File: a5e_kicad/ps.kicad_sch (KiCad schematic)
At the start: 51 parts, among them U15 TDA38812XUMA1

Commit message: Add LCSC part numbers and fix C102 footprint
Add a hidden LCSC field to 290 symbols from the JLCPCB parts match
(2026-10-23). Left without LCSC: U7, U15, L1 (not in the JLCPCB
library), C1/C2/C4 and L2-L5 (no value specified), J3 (no confident
match) and Y3 (the 12 pF Basic crystal does not suit the 27 pF load
caps). U2, U12, Y2 and J9 carry the exact-MPN LCSC numbers although
they currently show zero JLCPCB stock.

C102 (22U 6V3) had a 0201 footprint; no 22 uF 0201 part exists. Change
it to 0402 (C415703) like C5-C7.
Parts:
- C122, C133, C134, C135, C136, C137, C138, C139, C140, C141, C142, C143, C144, C145, C146, C147, C148, C149, C150, C151, C152, C153, C154, C155, C156: LCSC (none) -> C190183
- C123, C129, C130, C131, C132, C5, C6, C7: LCSC (none) -> C415703
- C124: LCSC (none) -> C84494
- C198: LCSC (none) -> C1530
- C199, C200: LCSC (none) -> C327019
- C201, C224, C225, C226, C227: LCSC (none) -> C12530
- C202: LCSC (none) -> C1525
- R1: LCSC (none) -> C25783
- R2: LCSC (none) -> C25744
- R55, R58: LCSC (none) -> C25908
- R56: LCSC (none) -> C132339
- R57: LCSC (none) -> C36871

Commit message: VCORE: PGOOD pull-up off 5V0 (abs max 4 V), L1 rated for the OCP limit
Checked the TDA38812 stage against its data sheet (V2.1). MODE gives
1 MHz FCCM, OCP valley is 10.7 A typ / 12.4 A max with R55 5.6k,
soft-start is 2.2 ms, and the output is 0.754 V; the load is 6-7 A worst
case per Quartus.

- R58: PGOOD was pulled to 5V0, but its absolute maximum is 4.0 V. It is
  now 10k (>= 10k per the data sheet) to the TDA38812 VCC LDO (3.0 V,
  net tda_vcc). The AP61202 EN threshold is 0.91 V.
- L1: needs Isat >= OCPmax + ripple ~ 15.3 A. The Cyntec CMLE051H had no
  LCSC number and an unknown rating. It is now the Tai-Tech
  TMPC0503H-R22MG-D (C357176, 220 nH, Isat 21 A, 3.7 mOhm), with a new
  footprint agilex_lib:L_TaiTech_TMPC0503H from the data sheet land
  pattern.
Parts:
- L1: value 250n -> 220n; footprint agilex_lib:CMLE051H -> agilex_lib:L_TaiTech_TMPC0503H; LCSC (none) -> C357176
- R58: value 5.6k -> 10k; LCSC C25908 -> C25744
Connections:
- net 5V0: no longer R58.1
- net tda_vcc: now reaches C201.2, U15.19 (VCC)
- net tda_vcc: now also R58.1
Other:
- note added: "R58 PGOOD pull-up to the TDA38812 VCC LDO (3.0 V): PGOOD abs max is 4.0 V, so not 5V0. L1: Isat >= OCPmax + ripple = 12.4 A + 2.9 A (R55 5.6k, 1 MHz FCCM via R56||R57 = 60.6k)"
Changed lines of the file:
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@@
 	)
 	(junction
-		(at 100.33 60.96)
-		(diameter 0)
-		(color 0 0 0 0)
-	)
-	(junction
 		(at 208.28 44.45)
 		(diameter 0)
@@
 	(wire
 		(pts
-			(xy 100.33 67.31) (xy 100.33 60.96)
-		)
-		(stroke
-			(width 0)
-			(type default)
-		)
-	)
-	(wire
-		(pts
 			(xy 128.27 137.16) (xy 148.59 137.16)
 		)
@@
 			)
 		)
-		(property "Value" "250n"
+		(property "Value" "220n"
 			(at 195.58 68.58 90)
 			(show_name no)
@@
 			)
 		)
-		(property "Footprint" "agilex_lib:CMLE051H"
+		(property "LCSC" "C357176"
+			(at 195.58 71.12 0)
+			(hide yes)
+			(show_name no)
+			(do_not_autoplace no)
+			(effects
+				(font
+					(size 1.27 1.27)
+				)
+			)
+		)
+		(property "Footprint" "agilex_lib:L_TaiTech_TMPC0503H"
 			(at 195.58 71.12 0)
 			(hide yes)
@@
 			)
 		)
-		(property "Description" "Inductor"
+		(property "Description" "Tai-Tech TMPC0503H-R22MG-D, 220 nH, Isat 21 A, Irms 15.5 A, 3.7 mOhm"
 			(at 195.58 71.12 0)
 			(hide yes)
@@
 			)
 		)
-		(property "Value" "5.6k"
+		(property "Value" "10k"
 			(at 102.87 72.3899 0)
 			(show_name no)
@@
 			)
 		)
-		(property "LCSC" "C25908"
+		(property "LCSC" "C25744"
 			(at 98.552 71.12 90)
 			(hide yes)
@@
 		)
 	)
+	(wire
+		(pts
+			(xy 100.33 67.31) (xy 100.33 64.77)
+		)
+		(stroke
+			(width 0)
+			(type default)
+		)
+	)
+	(label "tda_vcc"
+		(at 100.33 64.77 0)
+		(effects
+			(font
+				(size 1.27 1.27)
+			)
+			(justify left bottom)
+		)
+	)
+	(label "tda_vcc"
+		(at 123.19 64.77 0)
+		(effects
+			(font
+				(size 1.27 1.27)
+			)
+			(justify left bottom)
+		)
+	)
+	(text "R58 PGOOD pull-up to the TDA38812 VCC LDO (3.0 V): PGOOD abs max is 4.0 V, so not 5V0.\nL1: Isat >= OCPmax + ripple = 12.4 A + 2.9 A (R55 5.6k, 1 MHz FCCM via R56||R57 = 60.6k)"
+		(exclude_from_sim no)
+		(at 60.96 40.64 0)
+		(effects
+			(font
+				(size 1.27 1.27)
+			)
+			(justify left)
+		)
+	)

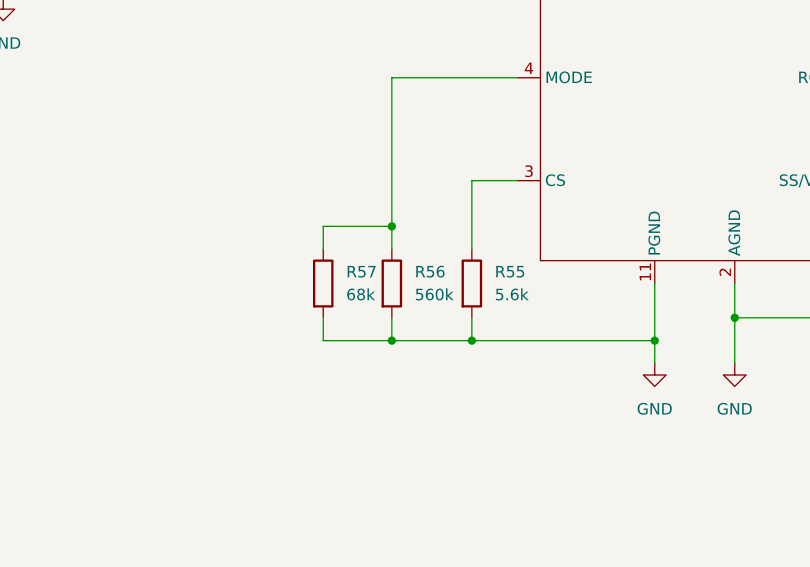
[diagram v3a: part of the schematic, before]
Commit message: Add jlc-tools submodule; fix two parts JLC can't supply
- tools/jlc: johonkanen/jlc-tools (06e4105). Part search, BOM stock
  check, BOM/CPL and fab outputs, as on the Agilex 3 card.
- The stock check (orderable quantity, 10 boards) found:
  - R56 560k (C132339) oversold, min buy 10000. R56 is now DNP and R57
    is a single 60.4k 1% (C25911): the TDA38812 data sheet value for
    1 MHz FCCM, same as the old 560k||68k = 60.6k.
  - Y2 SIT8924BA-73-18N (C17359088): 0 free. Changed to
    SIT8924BA-78-18E (C17247134, 1000 free), same 2016 footprint. Pin 1
    is OE on this variant and is left open (output enabled).
- Still open: J9 RJ45 RB1-125B8G1A (C363353) is oversold.
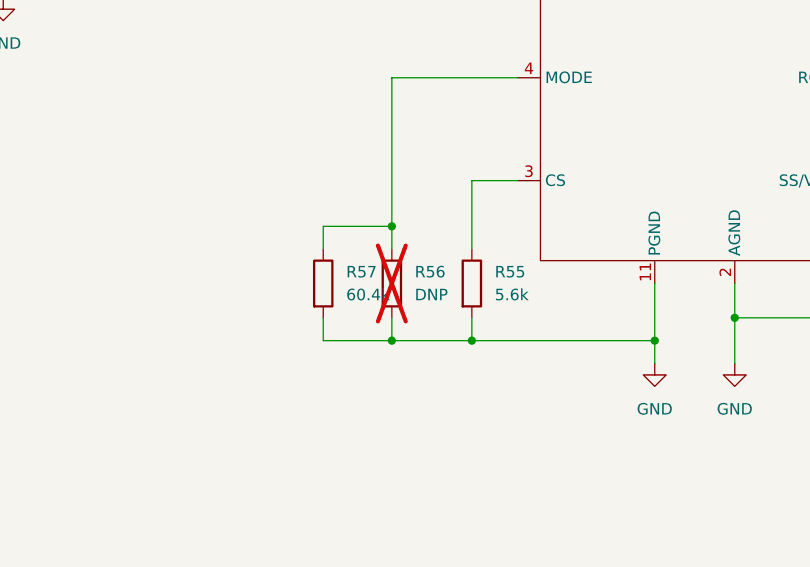
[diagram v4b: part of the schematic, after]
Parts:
- R56: value 560k -> DNP; LCSC C132339 -> (none); now not fitted
- R57: value 68k -> 60.4k; LCSC C36871 -> C25911
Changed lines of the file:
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@@
 			)
 		)
-		(property "Value" "68k"
+		(property "Value" "60.4k"
 			(at 114.3 132.0799 0)
 			(show_name no)
@@
 			)
 		)
-		(property "LCSC" "C36871"
+		(property "LCSC" "C25911"
 			(at 109.982 130.81 90)
 			(hide yes)
@@
 		(on_board yes)
 		(in_pos_files yes)
-		(dnp no)
+		(dnp yes)
 		(fields_autoplaced yes)
 		(property "Reference" "R56"
@@
 			)
 		)
-		(property "Value" "560k"
+		(property "Value" "DNP"
 			(at 121.92 132.0799 0)
 			(show_name no)
@@
 			)
 		)
-		(property "LCSC" "C132339"
+		(property "LCSC" ""
 			(at 117.602 130.81 90)
 			(hide yes)

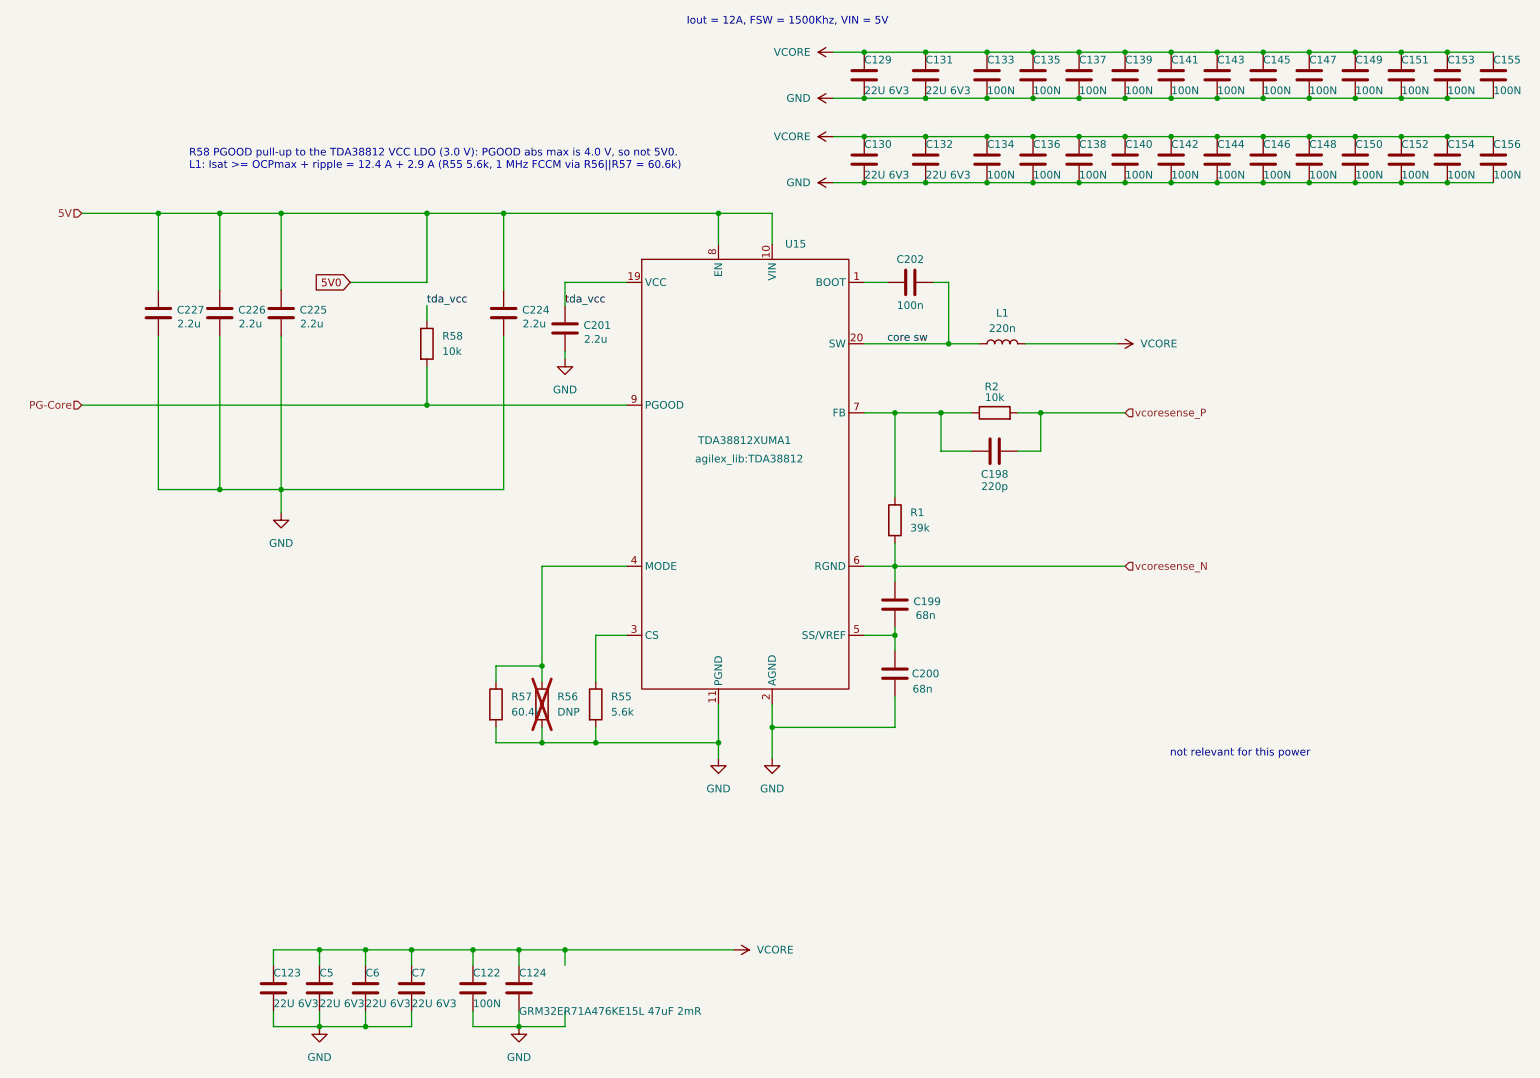
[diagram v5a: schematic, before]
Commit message: VCORE: U15 TDA38812 -> TPS548A28 (JLC C5219375), checklist updated
The TDA38812 is not available at JLC. The TI TPS548A28 has the same
VQFN-HR-21 3x4 land pattern and pin functions (CS->TRIP, SS/VREF->SS/REFIN,
RGND->VSNS-); footprint kept, new symbol agilex_5_lib:TPS548A28.
MODE 60.4k (1 MHz FCCM), TRIP 5.6k (10.7 A valley), soft-start, PGOOD
pull-up, L1 and output caps carry over.
- FB divider R2 2.55k / R1 10k -> 0.753 V (TI: bottom 1-20k)
- C198 feed-forward DNP
- EN no longer tied to 5V0: R291 24.3k / R292 10k (on at VIN 4.2 V)
- C266/C267 1 uF X6S 0402 at the VIN pads
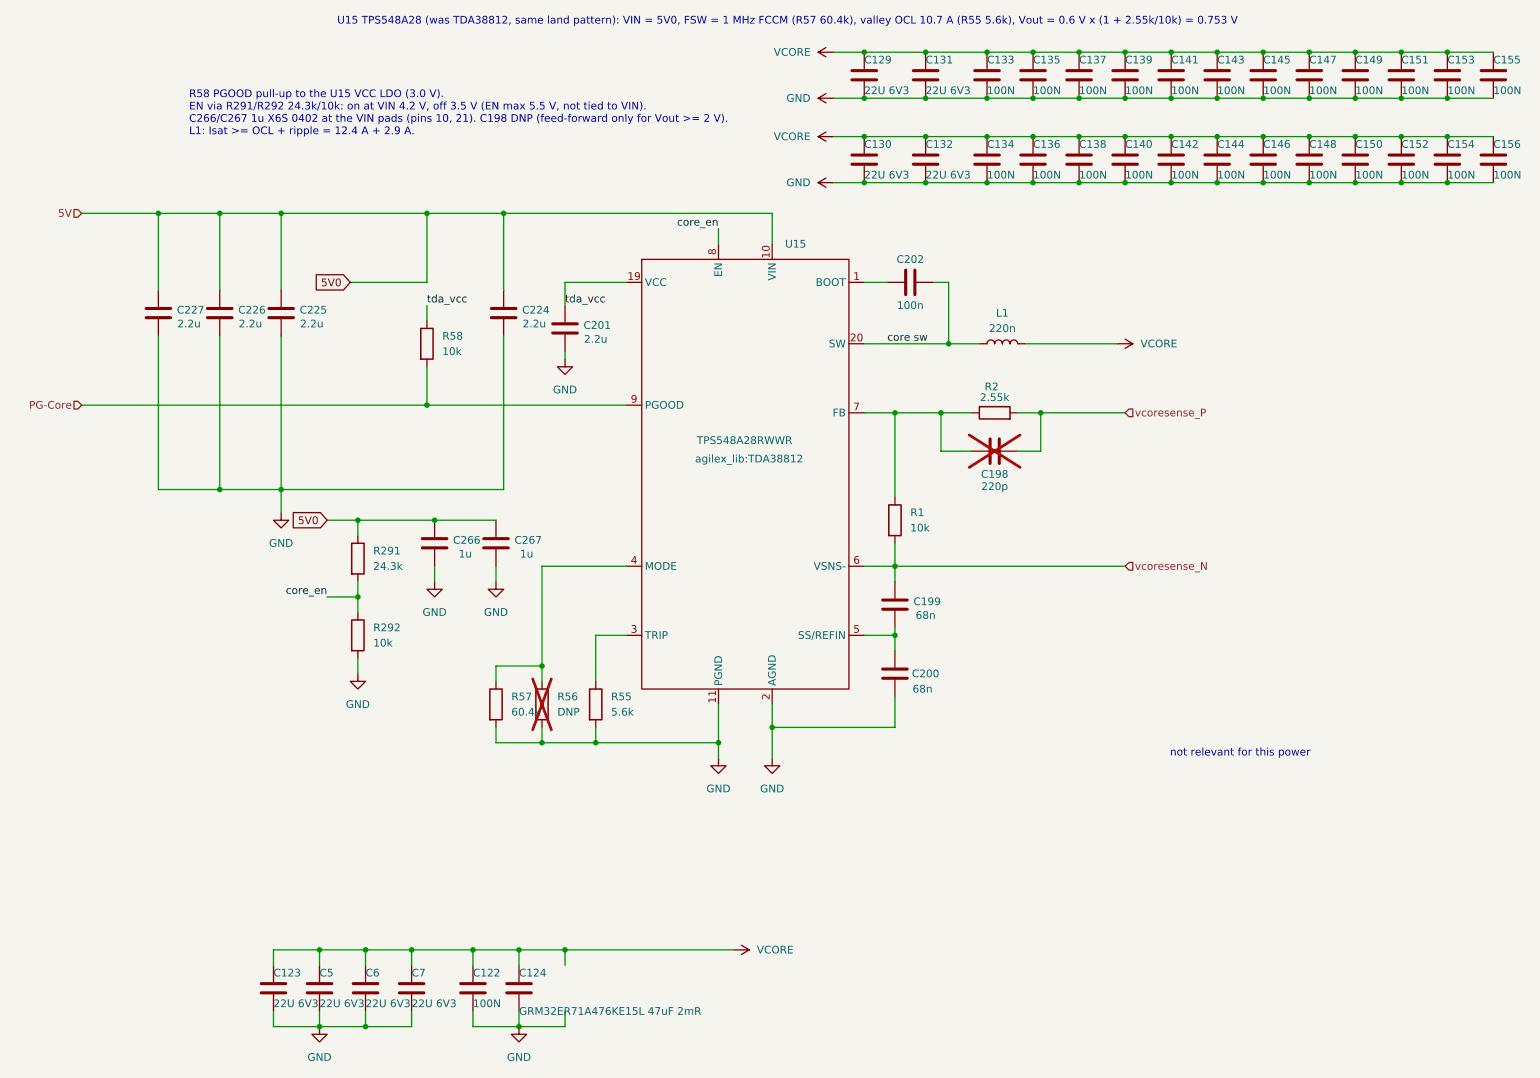
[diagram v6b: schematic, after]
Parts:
- added C266, C267: 1u, Capacitor_SMD:C_0402_1005Metric, symbol Device:C
- added R291: 24.3k, Resistor_SMD:R_0402_1005Metric, symbol Device:R
- added R292: 10k, Resistor_SMD:R_0402_1005Metric, symbol Device:R
- C198: now not fitted
- R1: value 39k -> 10k; LCSC C25783 -> C25744
- R2: value 10k -> 2.55k; LCSC C25744 -> C95596
- U15: value TDA38812XUMA1 -> TPS548A28RWWR; symbol agilex_5_lib:TDA38812 -> agilex_5_lib:TPS548A28; LCSC (none) -> C5219375
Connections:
- net 5V0: now also C266.2, C267.2, R291.1; no longer U15.8 (EN)
- net GND: now also C266.1, C267.1, R292.2
- new net core_en: R291.2, R292.1, U15.8 (EN)
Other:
- note added: "R58 PGOOD pull-up to the U15 VCC LDO (3.0 V). EN via R291/R292 24.3k/10k: on at VIN 4.2 V, off 3.5 V (EN max 5.5 V, not tied to VIN). C266/C267 1u X6S 0402 at the VIN pads (pins 10, 21). C198 DNP (feed-forward only for Vout >= 2 V). L1: Isat >= OCL + ripple = 12.4 A + 2.9 A."
- note added: "U15 TPS548A28 (was TDA38812, same land pattern): VIN = 5V0, FSW = 1 MHz FCCM (R57 60.4k), valley OCL 10.7 A (R55 5.6k), Vout = 0.6 V x (1 + 2.55k/10k) = 0.753 V"
- note removed: "Iout = 12A, FSW = 1500Khz, VIN = 5V"
- note removed: "R58 PGOOD pull-up to the TDA38812 VCC LDO (3.0 V): PGOOD abs max is 4.0 V, so not 5V0. L1: Isat >= OCPmax + ripple = 12.4 A + 2.9 A (R55 5.6k, 1 MHz FCCM via R56||R57 = 60.6k)"
